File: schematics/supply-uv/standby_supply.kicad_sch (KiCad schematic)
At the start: 37 parts, among them Q10 IRLML5203, U24 TL432DBZ, U3 R7731, U4 EL817

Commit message: Found and fixed issues in schematics.
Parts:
- removed C4: 22 uF@50V, Capacitor_THT:CP_Radial_D5.0mm_P2.00mm, symbol Device:C_Polarized
- added C16: 22 uF, Capacitor_SMD:C_1210_3225Metric, symbol Device:C
- added R10: 1R, Resistor_SMD:R_2512_6332Metric, symbol Device:R
- added TP2: STB VCC, TestPoint:TestPoint_Pad_2.0x2.0mm, symbol Connector:TestPoint
- added TP2: Supply VCC, TestPoint:TestPoint_Pad_2.0x2.0mm, symbol Connector:TestPoint
- R12: value 1K -> 150
- R13: value 1K2 -> NOT INSTALLED
- R14: value 20K -> 22K
- R15: value 4K7 -> 2K2
- R18: value 200K -> 100K
- R8: value 305K -> 220K
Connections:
- net HV_GND: now also C16.1, R10.1; no longer QP1.3 (S), R10.1
- net at D3.1 (K), R7.1, U3.5 (VDD): now also C16.2, TP2.1
- net at C10.1, D1.2 (A), JP2.1 (A)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: now also TP2.1
- new net: QP1.3 (S), R10.1, R10.2

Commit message: standby & pfc almost works
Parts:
- R10: value 10K -> 5
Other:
- note added: "OUTPUT: 13.6V, 0.5A UN-ISOLATED !"
- note removed: "OUTPUT: 13.5V, 0.5A UN-ISOLATED !"
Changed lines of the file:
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@@
     (effects (font (size 1.27 1.27)) (justify left bottom))
   )
-  (text "OUTPUT:\n13.5V, 0.5A\nUN-ISOLATED !" (at 222.25 39.37 0)
+  (text "OUTPUT:\n13.6V, 0.5A\nUN-ISOLATED !" (at 222.25 39.37 0)
     (effects (font (size 5 5) (thickness 1) bold) (justify left bottom))
   )
@@
       (effects (font (size 1.27 1.27)) (justify left))
     )
-    (property "Value" "10K" (at 81.28 109.22 90)
-      (effects (font (size 1.27 1.27)) (justify left))
-    )
+    (property "Value" "5" (at 81.28 109.22 90)
+      (effects (font (size 1.27 1.27)) (justify left))
+    )

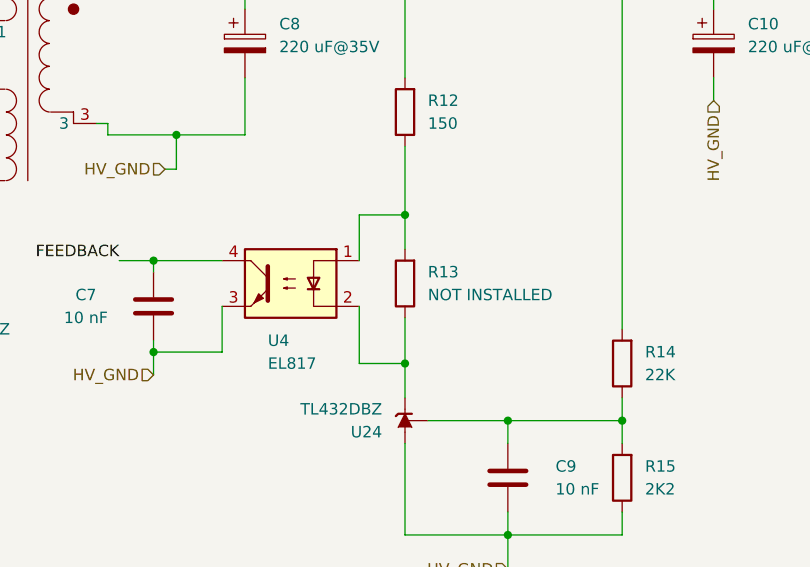
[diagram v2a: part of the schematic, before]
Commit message: fix pins in firmware
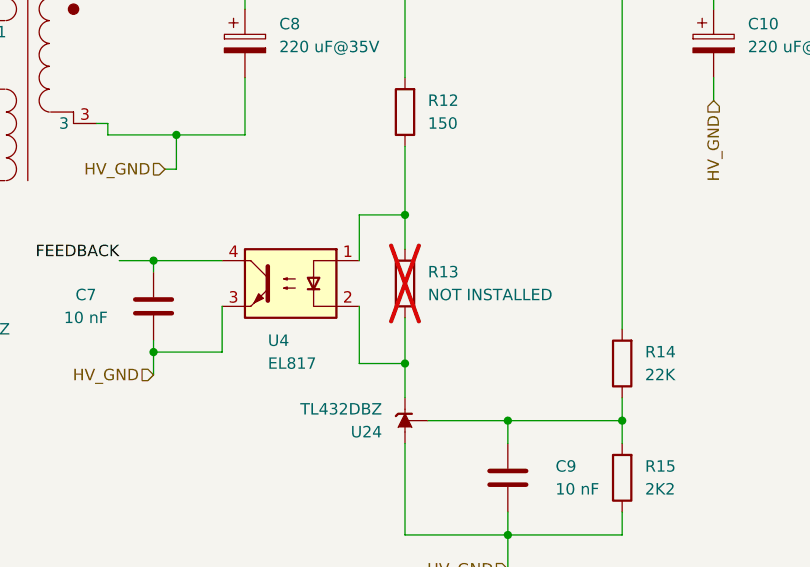
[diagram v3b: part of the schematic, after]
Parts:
- R13: now not fitted
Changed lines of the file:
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@@
   )
   (symbol (lib_id "Device:R") (at 153.67 100.33 180) (unit 1)
-    (in_bom yes) (on_board yes) (dnp no) (fields_autoplaced)
+    (in_bom yes) (on_board yes) (dnp yes) (fields_autoplaced)
     (property "Reference" "R13" (at 156.21 99.06 0)
       (effects (font (size 1.27 1.27)) (justify right))

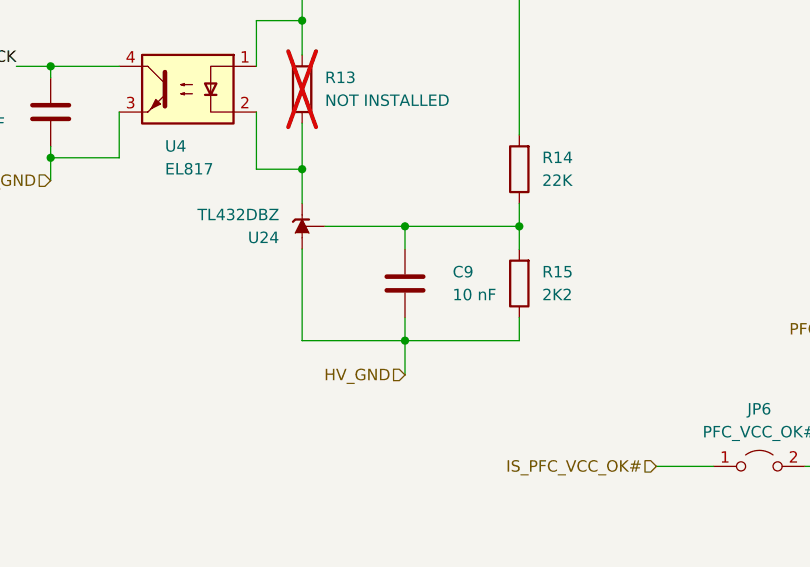
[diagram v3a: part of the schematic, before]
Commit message: supply board - power controllers changed; PWM logic changed
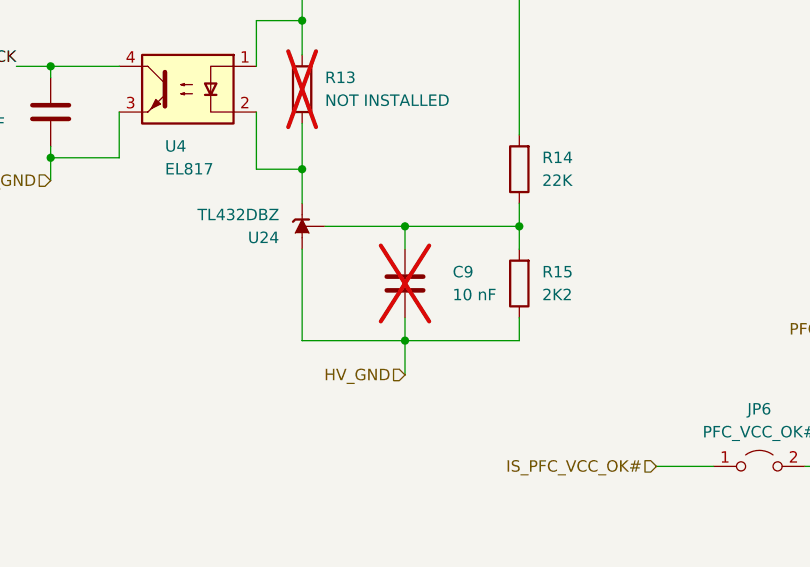
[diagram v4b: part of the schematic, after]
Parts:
- C9: now not fitted
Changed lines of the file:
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@@
   )
   (symbol (lib_id "Device:C") (at 165.1 121.92 180) (unit 1)
-    (in_bom yes) (on_board yes) (dnp no)
+    (in_bom yes) (on_board yes) (dnp yes)
     (property "Reference" "C9" (at 172.72 120.65 0)
       (effects (font (size 1.27 1.27)) (justify left))

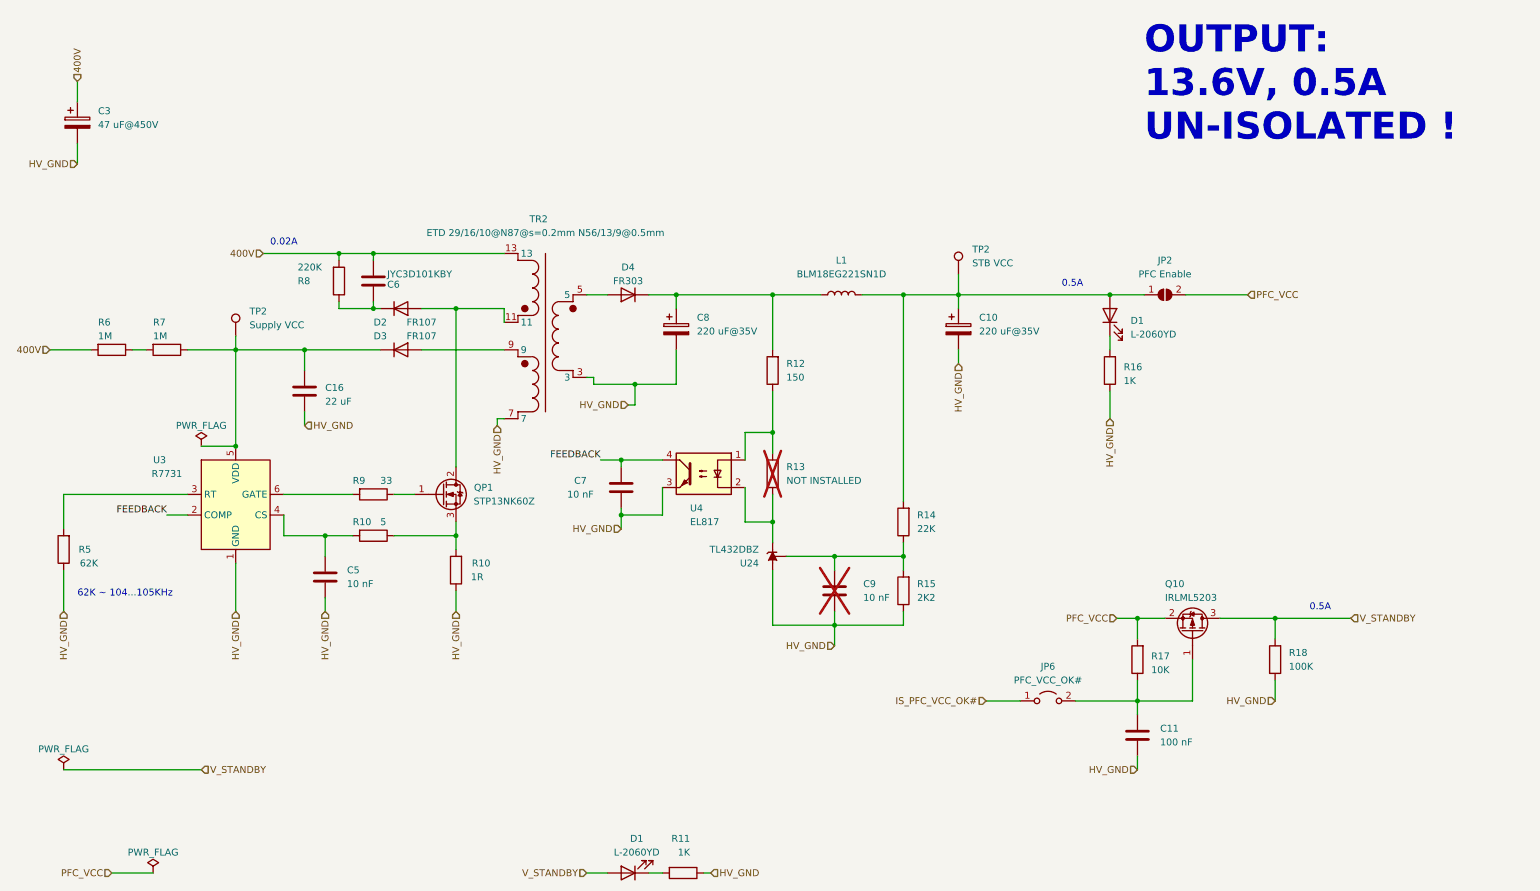
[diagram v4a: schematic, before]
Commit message: some changes in schema. I found additional error. This commit saves changes before re-write some blocks
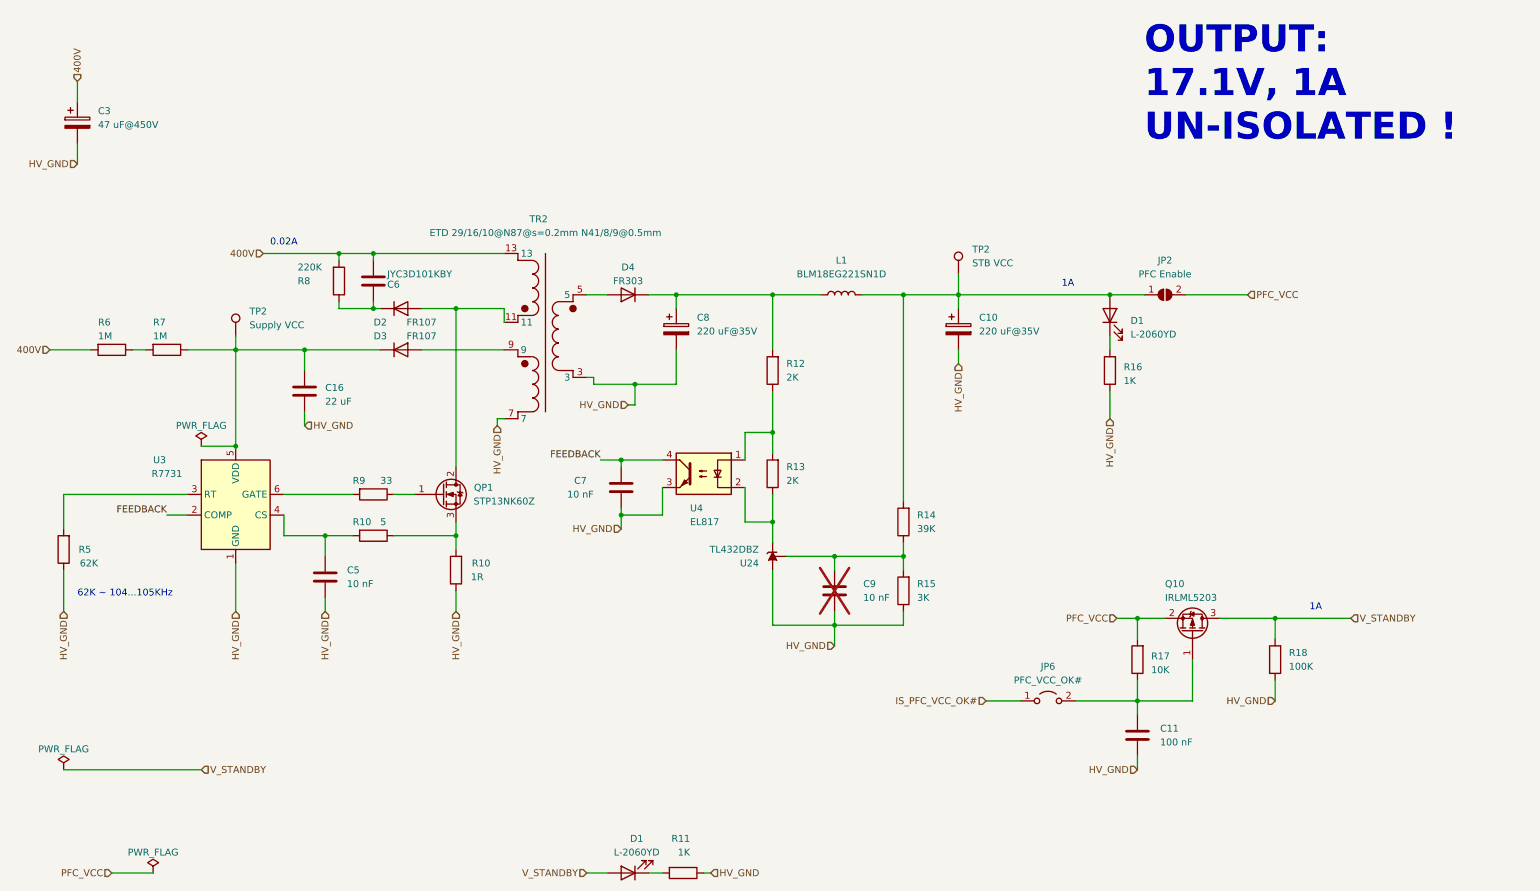
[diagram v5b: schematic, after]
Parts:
- R12: value 150 -> 2K
- R13: value NOT INSTALLED -> 2K; now fitted
- R14: value 22K -> 39K
- R15: value 2K2 -> 3K
- TR2: value ETD 29/16/10@N87@s=0.2mm N56/13/9@0.5mm -> ETD 29/16/10@N87@s=0.2mm N41/8/9@0.5mm
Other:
- note added: "1A"
- note added: "OUTPUT: 17.1V, 1A UN-ISOLATED !"
- note removed: "0.5A"
- note removed: "OUTPUT: 13.6V, 0.5A UN-ISOLATED !"

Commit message: debugging DCDC converters... Standby supply works fine (noise level = 1,7%). At now Starting to debug PFC module
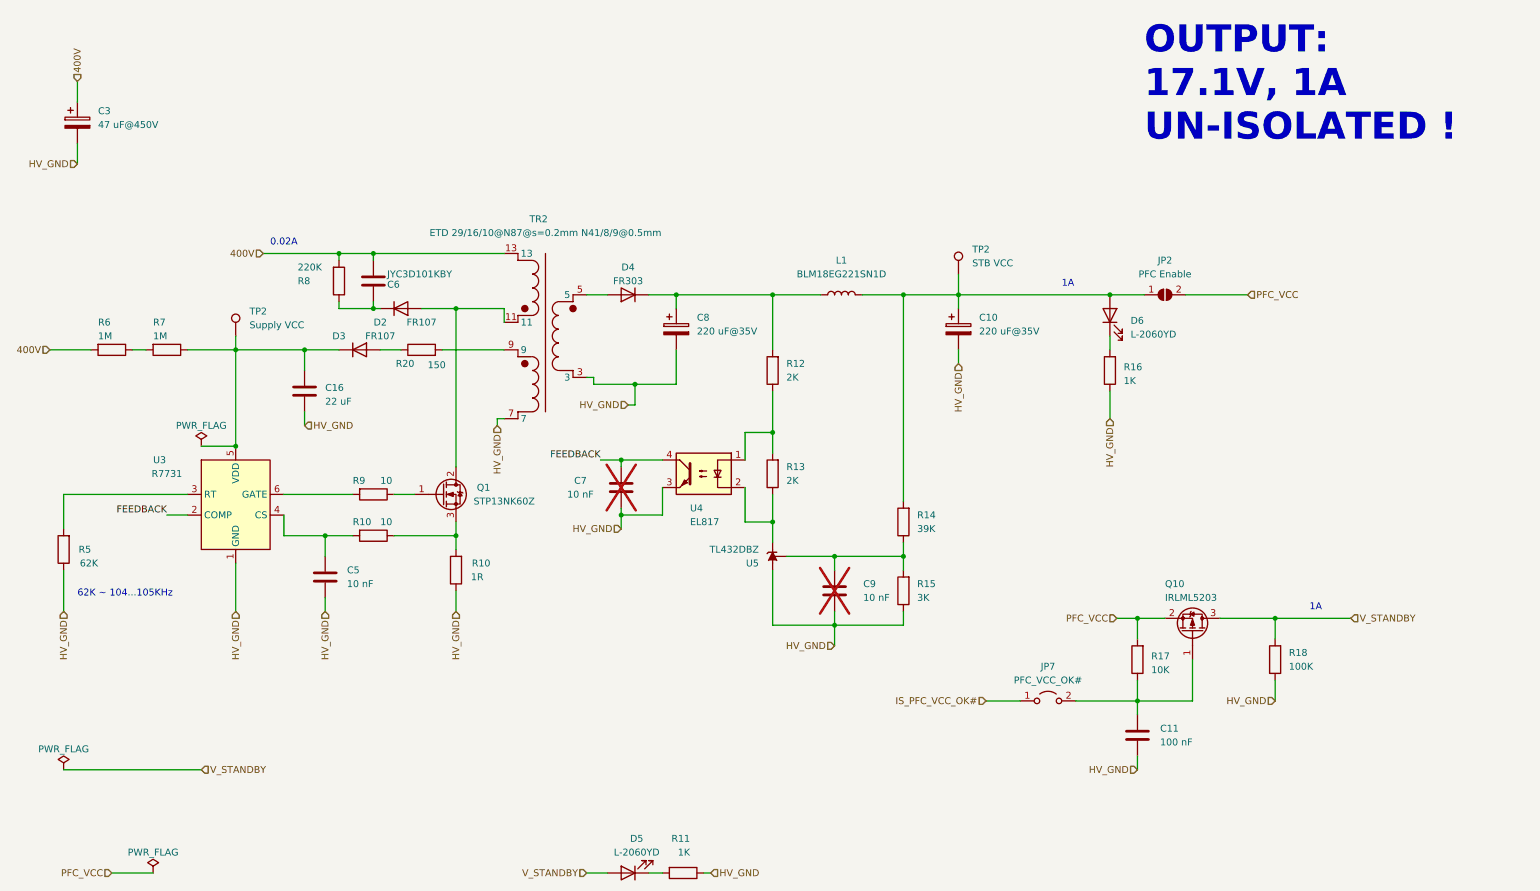
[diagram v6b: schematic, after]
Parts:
- added R20: 150, Resistor_SMD:R_0805_2012Metric, symbol Device:R
- C7: now not fitted
- R10: value 5 -> 10
- R9: value 33 -> 10
- renumbered D1 to D5, D1 to D6, JP6 to JP7, QP1 to Q1, U24 to U5
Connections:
- net at D3.2 (A): now also R20.1; no longer TR2.9
- new net: R20.2, TR2.9
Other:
- moved on the sheet: D3
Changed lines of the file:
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@@
 	(wire
 		(pts
-			(xy 67.31 77.47) (xy 81.28 77.47)
+			(xy 67.31 77.47) (xy 73.66 77.47)
 		)
 		(stroke
@@
 	(wire
 		(pts
+			(xy 92.71 77.47) (xy 104.14 77.47)
+		)
+		(stroke
+			(width 0)
+			(type default)
+		)
+	)
+	(wire
+		(pts
 			(xy 153.67 67.31) (xy 153.67 77.47)
 		)
@@
 	(wire
 		(pts
+			(xy 81.28 77.47) (xy 85.09 77.47)
+		)
+		(stroke
+			(width 0)
+			(type default)
+		)
+	)
+	(wire
+		(pts
 			(xy 45.72 77.47) (xy 54.61 77.47)
 		)
@@
 	(wire
 		(pts
-			(xy 88.9 77.47) (xy 104.14 77.47)
-		)
-		(stroke
-			(width 0)
-			(type default)
-		)
-	)
-	(wire
-		(pts
 			(xy 165.1 128.27) (xy 177.8 128.27)
 		)
@@
 	(symbol
 		(lib_id "Device:D")
-		(at 85.09 77.47 0)
+		(at 77.47 77.47 0)
 		(unit 1)
 		(exclude_from_sim no)
@@
 		(dnp no)
 		(property "Reference" "D3"
-			(at 81.28 74.93 0)
+			(at 73.66 74.93 0)
 			(effects
 				(font
@@
 		)
 		(property "Value" "FR107"
-			(at 88.9 74.93 0)
+			(at 81.28 74.93 0)
 			(effects
 				(font
@@
 		)
 		(property "Footprint" "Diode_THT:D_DO-41_SOD81_P7.62mm_Horizontal"
-			(at 85.09 77.47 0)
+			(at 77.47 77.47 0)
 			(effects
 				(font
@@
 		)
 		(property "Datasheet" "~"
-			(at 85.09 77.47 0)
+			(at 77.47 77.47 0)
 			(effects
 				(font
@@
 		)
 		(property "Description" ""
-			(at 85.09 77.47 0)
+			(at 77.47 77.47 0)
 			(effects
 				(font
@@
 		)
 		(property "Sim.Device" "D"
-			(at 85.09 77.47 0)
+			(at 77.47 77.47 0)
 			(effects
 				(font
@@
 		)
 		(property "Sim.Pins" "1=K 2=A"
-			(at 85.09 77.47 0)
+			(at 77.47 77.47 0)
 			(effects
 				(font
@@
 			)
 		)
-		(property "Description" ""
+		(property "Description" "Special symbol for telling ERC where power comes from"
 			(at 48.26 95.25 0)
 			(effects
@@
 		(in_bom yes)
 		(on_board yes)
-		(dnp no)
+		(dnp yes)
 		(property "Reference" "C7"
 			(at 119.38 101.6 0)
@@
 			)
 		)
-		(property "Value" "33"
+		(property "Value" "10"
 			(at 81.28 101.6 90)
 			(effects
@@
 		(on_board yes)
 		(dnp no)
-		(property "Reference" "D1"
+		(property "Reference" "D5"
 			(at 128.5875 167.64 0)
 			(effects
@@
 		(instances
 			(project "supply"
-				(path "/1e139717-fcd1-4008-a6ea-4c993845e928/b56319b0-4827-4b6e-9ec0-247d1d8495e7"
-					(reference "D1")
-					(unit 1)
-				)
 				(path "/1e139717-fcd1-4008-a6ea-4c993845e928/07fd8385-9dfd-4a86-92c6-a09da3061b53"
 					(reference "D5")
 					(unit 1)
 				)
+				(path "/1e139717-fcd1-4008-a6ea-4c993845e928/b56319b0-4827-4b6e-9ec0-247d1d8495e7"
+					(reference "D1")
+					(unit 1)
+				)
 			)
 			(project "supply-uv"
@@
 			)
 		)
-		(property "Value" "5"
+		(property "Value" "10"
 			(at 81.28 109.22 90)
 			(effects
@@
 			)
 		)
-		(property "Description" ""
+		(property "Description" "-3.0A Id, -30V Vds, 98mOhm Rds, P-Channel HEXFET Power MOSFET, SOT-23"
 			(at 231.14 129.54 0)
 			(effects
@@
 			)
 			(project "supply"
-				(path "/1e139717-fcd1-4008-a6ea-4c993845e928/ce2ff71a-422a-4b17-921a-2433d38ec044"
-					(reference "Q10")
-					(unit 1)
-				)
 				(path "/1e139717-fcd1-4008-a6ea-4c993845e928/07fd8385-9dfd-4a86-92c6-a09da3061b53"
 					(reference "Q2")
 					(unit 1)
 				)
+				(path "/1e139717-fcd1-4008-a6ea-4c993845e928/ce2ff71a-422a-4b17-921a-2433d38ec044"
+					(reference "Q10")
+					(unit 1)
+				)
 			)
 			(project "supply-uv"
@@
 		(dnp no)
 		(fields_autoplaced yes)
-		(property "Reference" "JP6"
+		(property "Reference" "JP7"
 			(at 204.47 135.89 0)
 			(effects
@@
 		(instances
 			(project "supply"
-				(path "/1e139717-fcd1-4008-a6ea-4c993845e928/ce2ff71a-422a-4b17-921a-2433d38ec044"
-					(reference "JP6")
-					(unit 1)
-				)
 				(path "/1e139717-fcd1-4008-a6ea-4c993845e928/07fd8385-9dfd-4a86-92c6-a09da3061b53"
 					(reference "JP7")
 					(unit 1)
 				)
+				(path "/1e139717-fcd1-4008-a6ea-4c993845e928/ce2ff71a-422a-4b17-921a-2433d38ec044"
+					(reference "JP6")
+					(unit 1)
+				)
 			)
 			(project "supply-uv"
@@
 		(on_board yes)
 		(dnp no)
-		(property "Reference" "QP1"
+		(property "Reference" "Q1"
 			(at 100.33 102.87 0)
 			(effects
@@
 		(instances
 			(project "supply"
-				(path "/1e139717-fcd1-4008-a6ea-4c993845e928/b56319b0-4827-4b6e-9ec0-247d1d8495e7"
-					(reference "QP1")
-					(unit 1)
-				)
 				(path "/1e139717-fcd1-4008-a6ea-4c993845e928/07fd8385-9dfd-4a86-92c6-a09da3061b53"
 					(reference "Q1")
 					(unit 1)
 				)
+				(path "/1e139717-fcd1-4008-a6ea-4c993845e928/b56319b0-4827-4b6e-9ec0-247d1d8495e7"
+					(reference "QP1")
+					(unit 1)
+				)
 			)
 			(project "supply-uv"
@@
 		(dnp no)
 		(fields_autoplaced yes)
-		(property "Reference" "D1"
+		(property "Reference" "D6"
 			(at 219.71 72.0725 90)
 			(effects
@@
 		(instances
 			(project "supply"
-				(path "/1e139717-fcd1-4008-a6ea-4c993845e928/b56319b0-4827-4b6e-9ec0-247d1d8495e7"
-					(reference "D1")
-					(unit 1)
-				)
 				(path "/1e139717-fcd1-4008-a6ea-4c993845e928/07fd8385-9dfd-4a86-92c6-a09da3061b53"
 					(reference "D6")
 					(unit 1)
 				)
+				(path "/1e139717-fcd1-4008-a6ea-4c993845e928/b56319b0-4827-4b6e-9ec0-247d1d8495e7"
+					(reference "D1")
+					(unit 1)
+				)
 			)
 			(project "supply-uv"
@@
 			)
 		)
-		(property "Description" ""
+		(property "Description" "Special symbol for telling ERC where power comes from"
 			(at 39.37 173.99 0)
 			(effects
@@
 		(on_board yes)
 		(dnp no)
-		(property "Reference" "U24"
+		(property "Reference" "U5"
 			(at 151.13 116.84 90)
 			(effects
@@
 		(instances
 			(project "supply"
-				(path "/1e139717-fcd1-4008-a6ea-4c993845e928/bcabd54f-a555-4409-9a4f-89c20a3d7682"
-					(reference "U24")
-					(unit 1)
-				)
 				(path "/1e139717-fcd1-4008-a6ea-4c993845e928/07fd8385-9dfd-4a86-92c6-a09da3061b53"
 					(reference "U5")
 					(unit 1)
 				)
+				(path "/1e139717-fcd1-4008-a6ea-4c993845e928/bcabd54f-a555-4409-9a4f-89c20a3d7682"
+					(reference "U24")
+					(unit 1)
+				)
 			)
 			(project "supply-uv"
@@
 			)
 		)
-		(property "Description" ""
+		(property "Description" "Special symbol for telling ERC where power comes from"
 			(at 22.86 154.94 0)
 			(effects
@@
 					(unit 1)
 				)
+			)
+		)
+	)
+	(symbol
+		(lib_id "Device:R")
+		(at 88.9 77.47 90)
+		(unit 1)
+		(exclude_from_sim no)
+		(in_bom yes)
+		(on_board yes)
+		(dnp no)
+		(property "Reference" "R20"
+			(at 85.852 80.01 90)
+			(effects
+				(font
+					(size 1.27 1.27)
+				)
+			)
+		)
+		(property "Value" "150"
+			(at 91.694 80.264 90)
+			(effects
+				(font
+					(size 1.27 1.27)
+				)
+			)
+		)
+		(property "Footprint" "Resistor_SMD:R_0805_2012Metric"
+			(at 88.9 79.248 90)
+			(effects
+				(font
+					(size 1.27 1.27)
+				)
+				(hide yes)
+			)
+		)
+		(property "Datasheet" "~"
+			(at 88.9 77.47 0)
+			(effects
+				(font
+					(size 1.27 1.27)
+				)
+				(hide yes)
+			)
+		)
+		(property "Description" ""
+			(at 88.9 77.47 0)
+			(effects
+				(font
+					(size 1.27 1.27)
+				)
+				(hide yes)
+			)
+		)
+		(pin "1"
+		)
+		(pin "2"
+		)
+		(instances
+			(project "supply-uv"
+				(path "/ef40850c-d0bf-4cba-961b-9aba418f8e73/1d298a4f-cf0d-440c-81b9-131daf06c23a"
+					(reference "R20")
+					(unit 1)
+				)
